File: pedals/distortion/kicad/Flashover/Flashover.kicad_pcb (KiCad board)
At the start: 2 copper layers, 84 x 84 mm, 95 parts, among them J1 Input, J2 Output, J3 9V DC, J4 SWD, J5 MIDI In, J6 MIDI Out, J7 To control board, K1 G6K-2F-Y 5VDC, K2 G6K-2F-Y 5VDC, Q1 MMBT3904, Q2 MMBT3904, SW5 Footswitch, U1 LM741, U11 H11L1, U2 TL072, U3 L7805, U4 RP2040, U5 W25Q16JVSS, U6 AP2112K-3.3, U7 MCP45HV51-104, U8 MCP45HV51-103, U9 MCP45HV51-103, Y1 12MHz

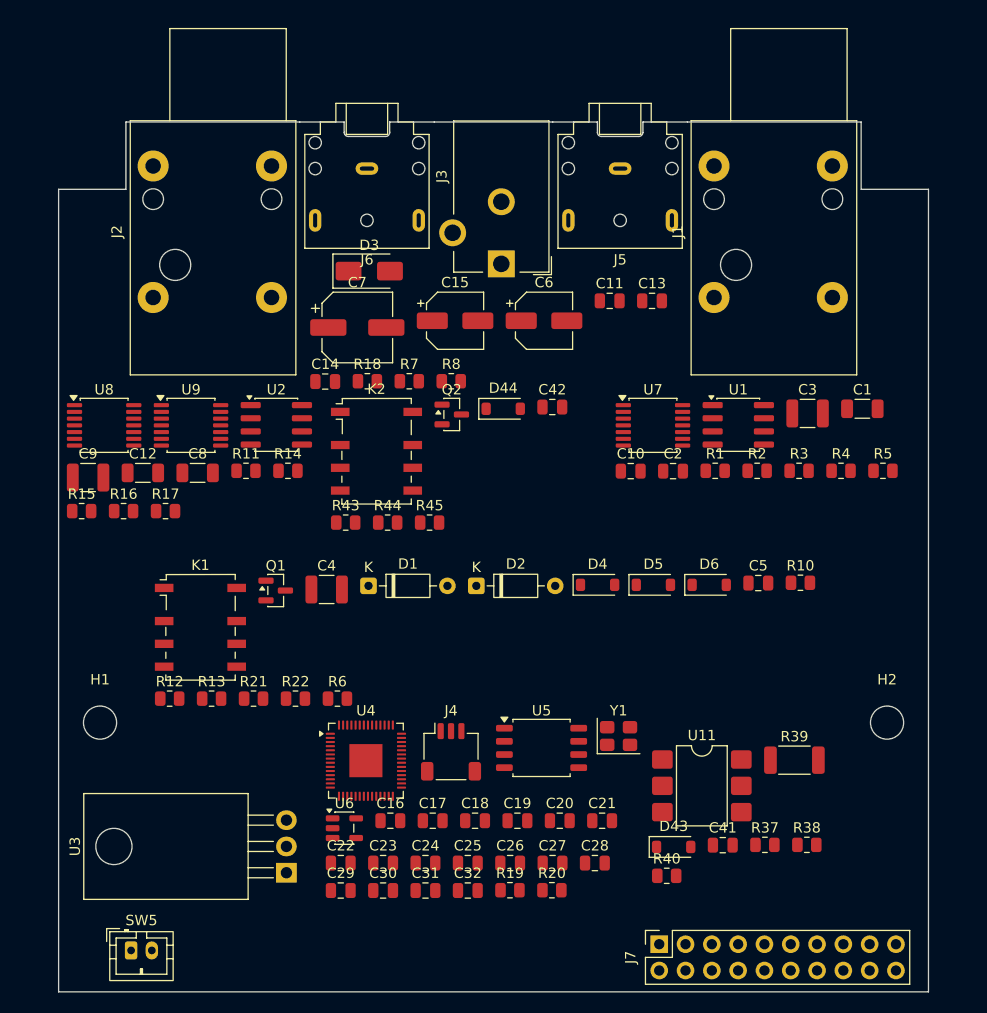
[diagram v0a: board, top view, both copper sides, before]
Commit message: Route Flashover boards (partial); add status note
Both boards now 4-layer with inner ground (and +5V) planes, JLCPCB-style
rules and net classes, ground/+5V via fan-out and autorouted signals.
Control board: 7 connections open.  Main board: 50 open; to be finished
by hand.  See pedals/distortion/kicad/FLASHOVER_STATUS.md.

Co-Authored-By: Claude Opus 5.5 <noreply@anthropic.com>
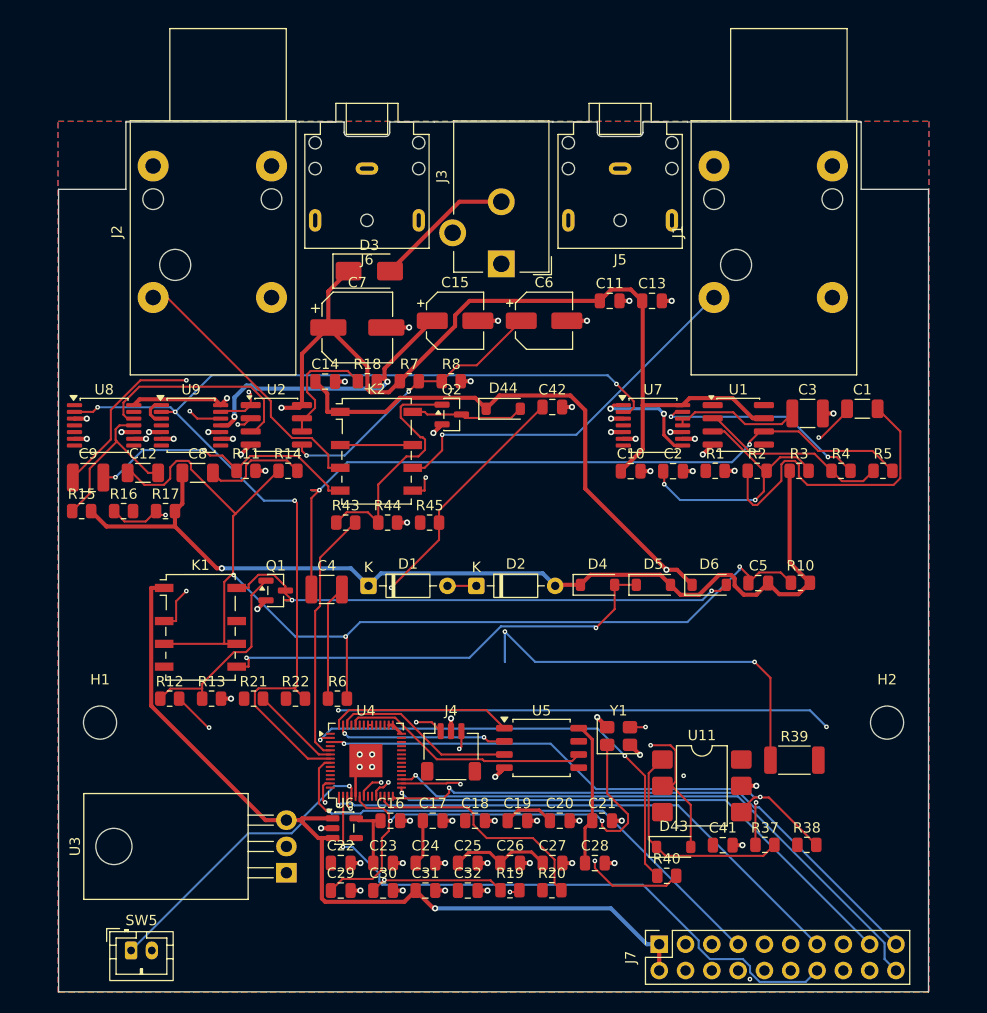
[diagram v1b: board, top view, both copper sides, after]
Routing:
- net +5V: track 0.00 -> 170.9 mm, vias 0 -> 2
- net +9V: track 0.00 -> 148.0 mm, vias 0 -> 2
- net VB: track 0.00 -> 143.7 mm, vias 0 -> 3
- net SCL: track 0.00 -> 109.5 mm, vias 0 -> 4
- net /Clipping/CLIP: track 0.00 -> 108.2 mm, vias 0 -> 3
- net Net-(J6-PadR): track 0.00 -> 90.3 mm, vias 0 -> 2
- net Net-(J6-PadT): track 0.00 -> 83.2 mm, vias 0 -> 1
- net LEVEL_SW: track 0.00 -> 80.8 mm, vias 0 -> 3
- net FOOTSW: track 0.00 -> 73.3 mm, vias 0 -> 2
- net /Clipping/GAIN_OUT: track 0.00 -> 72.4 mm, vias 0 -> 2
- net Net-(D43-A): track 0.00 -> 68.2 mm, vias 0 -> 1
- net GND: track 0.00 -> 68.0 mm, vias 0 -> 60
- net Net-(J5-PadR): track 0.00 -> 64.8 mm, vias 0 -> 1
- net LEVEL_B: track 0.00 -> 57.8 mm, vias 0 -> 1
- net LINK_LED: track 0.00 -> 56.6 mm, vias 0 -> 1
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- added copper zone on B.Cu, net GND
- added copper zone on F.Cu, net GND
- added copper zone on In1.Cu, net GND
- added copper zone on In2.Cu, net GND
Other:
- copper layers 2 -> 4

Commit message: Fit Flashover to the 1590BB and part datasheets
- Correct PEC11R encoder footprint (legs 13.2 mm apart) in a new
  GreywireStudio footprint library; swap it onto the control board and
  bend three tracks around the wider legs
- Move MIDI jacks to the side walls, spread the top jacks out and put
  their fronts against the wall; re-autoroute the main board
- gen_pcb.py rebuilds the control board only with --controls
- Add fit check, board heights and drilling guide to the status note;
  update the product document

Co-Authored-By: Claude Opus 5.5 <noreply@anthropic.com>
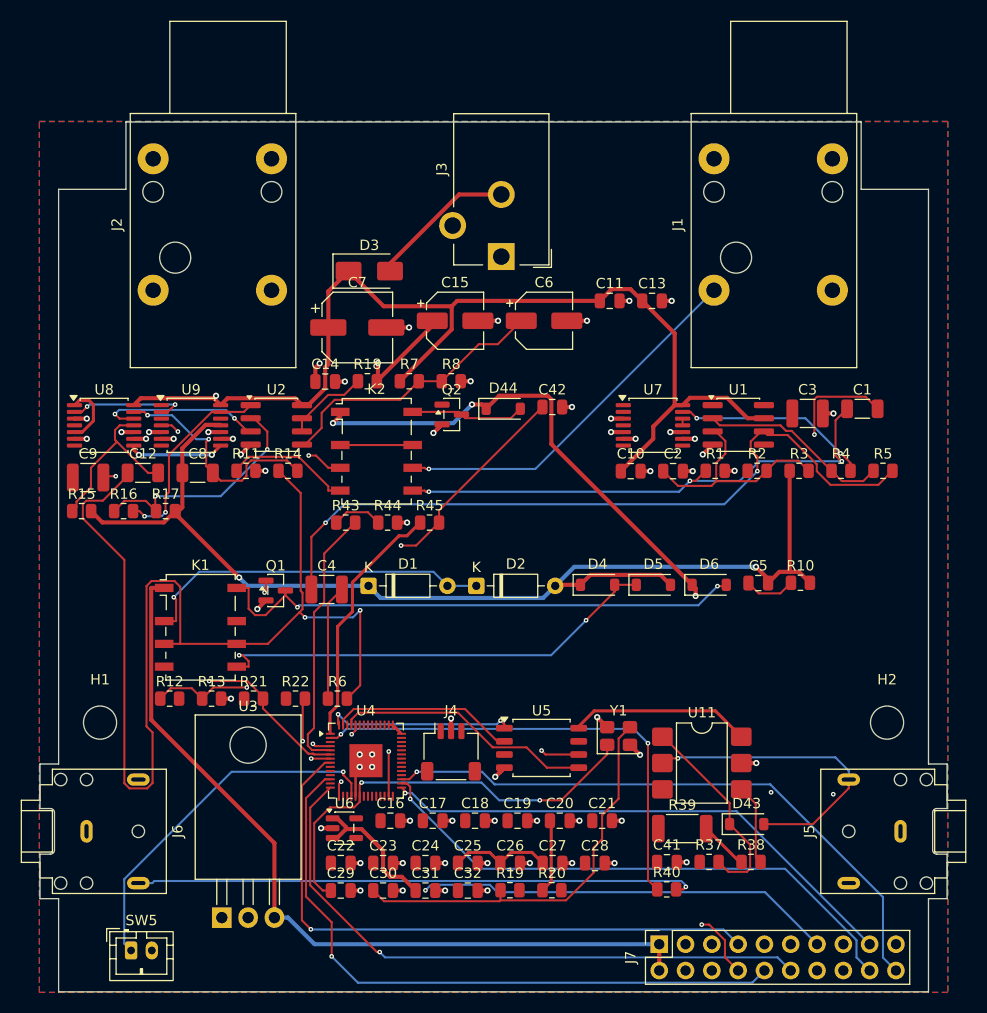
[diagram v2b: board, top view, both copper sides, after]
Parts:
- moved J5 69.5 mm to (186.3, 122.5), turned to 90 degrees
- moved J6 69.5 mm to (107.7, 122.5), turned to -90 degrees
- moved R39 12.7 mm to (165.2, 122.2)
- moved U3 7.60 mm to (120.8, 130.8), turned to 0 degrees
- moved D43 7.39 mm to (171.4, 121.8)
- moved R37 5.64 mm to (167.8, 125.5)
- moved C41 5.64 mm to (163.7, 125.5)
- moved R38 5.64 mm to (171.9, 125.5)
- moved U11 2.20 mm to (167.1, 115.9)
- moved R40 1.31 mm to (163.7, 128.1)
- moved J1 0.70 mm to (168.3, 70.2)
- moved J2 0.70 mm to (114.1, 70.2)
- moved J3 0.70 mm to (147.8, 67.0)
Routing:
- net Net-(J6-PadR): track 90.3 -> 0.00 mm, vias 2 -> 0
- net SCL: track 109.5 -> 19.7 mm
- net LEVEL_SW: track 80.8 -> 0.00 mm, vias 3 -> 0
- net Net-(J5-PadR): track 64.8 -> 0.00 mm, vias 1 -> 0
- net TONE_A: track 1.75 -> 62.7 mm
- net TONE_SW: track 0.00 -> 60.1 mm, vias 0 -> 1
- net LEVEL_B: track 57.8 -> 0.00 mm, vias 1 -> 0
- net LED_EN: track 55.6 -> 0.00 mm, vias 1 -> 0
- net LED_SCL: track 5.77 -> 54.4 mm
- net MIDI_RX: track 53.6 -> 7.78 mm, vias 2 -> 0
- net FX_IN: track 6.50 -> 50.5 mm, vias 2 -> 3
- net Net-(D43-A): track 68.2 -> 30.1 mm
- net SDA: track 8.73 -> 42.5 mm, vias 0 -> 2
- net Net-(J6-PadT): track 83.2 -> 54.4 mm
- net Net-(D1-A): track 7.25 -> 34.3 mm
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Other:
- board size 84 x 84 mm -> 87.6 x 84 mm

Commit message: Hand-route two Flashover main board connections; note progress
Connect Net-(C1-Pad2) and Net-(C3-Pad1) by hand (62 -> 60 open) and
record the next steps, including the planned route for the boxed-in
C9 connection, in FLASHOVER_STATUS.md.

Co-Authored-By: Claude Opus 5.5 <noreply@anthropic.com>
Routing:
- net Net-(C3-Pad1): track 0.65 -> 15.9 mm, vias 0 -> 2
- net Net-(C1-Pad2): track 10.1 -> 20.4 mm, vias 1 -> 2
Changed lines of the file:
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@@
+	)
+	(segment
+		(start 175.85 80.35)
+		(end 175.85 82.145)
+		(width 0.2)
+		(layer "F.Cu")
+		(net "Net-(C3-Pad1)")
+	)
+	(segment
+		(start 166.195 83.295)
+		(end 166.5 83.6)
+		(width 0.2)
+		(layer "F.Cu")
+		(net "Net-(C3-Pad1)")
+	)
+	(segment
+		(start 165.2575 83.295)
+		(end 166.195 83.295)
+		(width 0.2)
+		(layer "F.Cu")
+		(net "Net-(C3-Pad1)")
 	)
 	(segment
@@
 	)
 	(segment
+		(start 175.6 80.1)
+		(end 175.85 80.35)
+		(width 0.2)
+		(layer "F.Cu")
+		(net "Net-(C3-Pad1)")
+	)
+	(via
+		(at 175.6 80.1)
+		(size 0.45)
+		(drill 0.2)
+		(layers "F.Cu" "B.Cu")
+		(net "Net-(C3-Pad1)")
+	)
+	(via
+		(at 166.5 83.6)
+		(size 0.45)
+		(drill 0.2)
+		(layers "F.Cu" "B.Cu")
+		(net "Net-(C3-Pad1)")
+	)
+	(segment
+		(start 168.452748 80.1)
+		(end 175.6 80.1)
+		(width 0.2)
+		(layer "B.Cu")
+		(net "Net-(C3-Pad1)")
+	)
+	(segment
+		(start 166.1432 83.2432)
+		(end 166.1432 82.409548)
+		(width 0.2)
+		(layer "B.Cu")
+		(net "Net-(C3-Pad1)")
+	)
+	(segment
+		(start 166.5 83.6)
+		(end 166.1432 83.2432)
+		(width 0.2)
+		(layer "B.Cu")
+		(net "Net-(C3-Pad1)")
+	)
+	(segment
+		(start 166.1432 82.409548)
+		(end 168.452748 80.1)
+		(width 0.2)
+		(layer "B.Cu")
+		(net "Net-(C3-Pad1)")
+	)
+	(segment
 		(start 165.2575 81.995)
 		(end 166.0069 81.995)
@@
 	)
 	(segment
+		(start 171.5425 86.7425)
+		(end 170.8 86)
+		(width 0.2)
+		(layer "F.Cu")
+		(net "Net-(C1-Pad2)")
+	)
+	(segment
 		(start 178.2323 80.5314)
 		(end 177.9723 80.7914)
@@
 	)
 	(segment
+		(start 171.5425 87.685)
+		(end 171.5425 86.7425)
+		(width 0.2)
+		(layer "F.Cu")
+		(net "Net-(C1-Pad2)")
+	)
+	(segment
 		(start 184.09 81.695)
 		(end 182.9264 80.5314)
@@
 		(net "Net-(C1-Pad2)")
 	)
+	(via
+		(at 170.8 86)
+		(size 0.45)
+		(drill 0.2)
+		(layers "F.Cu" "B.Cu")
+		(net "Net-(C1-Pad2)")
+	)
+	(segment
+		(start 177.6006 83.8)
+		(end 177.989 84.1884)
+		(width 0.2)
+		(layer "B.Cu")
+		(net "Net-(C1-Pad2)")
+	)
+	(segment
+		(start 170.8 86)
+		(end 173 83.8)
+		(width 0.2)
+		(layer "B.Cu")
+		(net "Net-(C1-Pad2)")
+	)
+	(segment
+		(start 173 83.8)
+		(end 177.6006 83.8)
+		(width 0.2)
+		(layer "B.Cu")
+		(net "Net-(C1-Pad2)")
+	)

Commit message: Hand-route FX_OUT on the Flashover main board; note progress
Co-Authored-By: Claude Opus 5.5 <noreply@anthropic.com>
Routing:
- net FX_OUT: track 13.5 -> 25.5 mm, vias 1 -> 2
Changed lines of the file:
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@@
+	)
+	(segment
+		(start 121.335 87.6)
+		(end 122.0975 87.6)
+		(width 0.2)
+		(layer "F.Cu")
+		(net "FX_OUT")
 	)
 	(segment
 		(start 123.3557 86.333)
 		(end 122.1825 87.5062)
+		(width 0.2)
+		(layer "F.Cu")
+		(net "FX_OUT")
+	)
+	(segment
+		(start 122.0975 87.6)
+		(end 122.1825 87.685)
 		(width 0.2)
 		(layer "F.Cu")
@@
 		(net "FX_OUT")
 	)
+	(via
+		(at 121.335 87.6)
+		(size 0.45)
+		(drill 0.2)
+		(layers "F.Cu" "B.Cu")
+		(net "FX_OUT")
+	)
+	(segment
+		(start 110.5178 88.2092)
+		(end 111.127 87.6)
+		(width 0.2)
+		(layer "B.Cu")
+		(net "FX_OUT")
+	)
+	(segment
+		(start 111.127 87.6)
+		(end 121.335 87.6)
+		(width 0.2)
+		(layer "B.Cu")
+		(net "FX_OUT")
+	)

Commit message: Hand-route the boxed-in C9 connection on the Flashover main board
Co-Authored-By: Claude Opus 5.5 <noreply@anthropic.com>
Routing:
- net Net-(C9-Pad1): track 0.00 -> 19.3 mm, vias 0 -> 2
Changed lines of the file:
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@@
+	)
+	(segment
+		(start 106.37 88.335)
+		(end 106.37 86.43)
+		(width 0.2)
+		(layer "F.Cu")
+		(net "Net-(C9-Pad1)")
+	)
+	(segment
+		(start 120.622299 82.670201)
+		(end 120.6475 82.645)
+		(width 0.2)
+		(layer "F.Cu")
+		(net "Net-(C9-Pad1)")
+	)
+	(segment
+		(start 106.37 86.43)
+		(end 106.4 86.4)
+		(width 0.2)
+		(layer "F.Cu")
+		(net "Net-(C9-Pad1)")
+	)
+	(segment
+		(start 119.794351 82.670201)
+		(end 120.622299 82.670201)
+		(width 0.2)
+		(layer "F.Cu")
+		(net "Net-(C9-Pad1)")
+	)
+	(via
+		(at 106.4 86.4)
+		(size 0.45)
+		(drill 0.2)
+		(layers "F.Cu" "B.Cu")
+		(net "Net-(C9-Pad1)")
+	)
+	(via
+		(at 119.794351 82.670201)
+		(size 0.45)
+		(drill 0.2)
+		(layers "F.Cu" "B.Cu")
+		(net "Net-(C9-Pad1)")
+	)
+	(segment
+		(start 120.01 82.88585)
+		(end 119.794351 82.670201)
+		(width 0.2)
+		(layer "B.Cu")
+		(net "Net-(C9-Pad1)")
+	)
+	(segment
+		(start 120.01 84.787152)
+		(end 120.01 82.88585)
+		(width 0.2)
+		(layer "B.Cu")
+		(net "Net-(C9-Pad1)")
+	)
+	(segment
+		(start 107.655 85.145)
+		(end 119.652152 85.145)
+		(width 0.2)
+		(layer "B.Cu")
+		(net "Net-(C9-Pad1)")
+	)
+	(segment
+		(start 106.4 86.4)
+		(end 107.655 85.145)
+		(width 0.2)
+		(layer "B.Cu")
+		(net "Net-(C9-Pad1)")
+	)
+	(segment
+		(start 119.652152 85.145)
+		(end 120.01 84.787152)
+		(width 0.2)
+		(layer "B.Cu")
+		(net "Net-(C9-Pad1)")
 	)
 	(segment

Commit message: Hand-route CLIP on the Flashover main board; audio path done
Co-Authored-By: Claude Opus 5.5 <noreply@anthropic.com>
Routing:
- net /Clipping/CLIP: track 115.4 -> 155.2 mm
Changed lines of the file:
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@@
+	)
+	(segment
+		(start 134.1221 101.151)
+		(end 135.5637 102.5926)
+		(width 0.2)
+		(layer "F.Cu")
+		(net "/Clipping/CLIP")
 	)
 	(segment
@@
 		(width 0.2)
 		(layer "F.Cu")
+		(net "/Clipping/CLIP")
+	)
+	(segment
+		(start 135.5637 102.5926)
+		(end 167.5474 102.5926)
+		(width 0.2)
+		(layer "F.Cu")
+		(net "/Clipping/CLIP")
+	)
+	(segment
+		(start 167.5474 102.5926)
+		(end 171.615 98.525)
+		(width 0.2)
+		(layer "F.Cu")

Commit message: Route +1V1/+3V3 around U4's top pins; logic power uses 0.2 mm tracks
The 0.3 mm logic-power width and 0.6 mm vias can't escape the RP2040's
0.4 mm-pitch pins, so the class now uses the signal sizes.

Co-Authored-By: Claude Opus 5.5 <noreply@anthropic.com>
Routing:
- net /Controller/+1V1: track 9.89 -> 22.7 mm, vias 0 -> 2
- net +3V3: track 70.8 -> 74.4 mm
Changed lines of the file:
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@@
 	)
 	(setup
+		(stackup
+			(layer "F.SilkS"
+				(type "Top Silk Screen")
+			)
+			(layer "F.Paste"
+				(type "Top Solder Paste")
+			)
+			(layer "F.Mask"
+				(type "Top Solder Mask")
+				(thickness 0.01)
+			)
+			(layer "F.Cu"
+				(type "copper")
+				(thickness 0.035)
+			)
+			(layer "dielectric 1"
+				(type "core")
+				(thickness 0.48)
+				(material "FR4")
+				(epsilon_r 4.5)
+				(loss_tangent 0.02)
+			)
+			(layer "In1.Cu"
+				(type "copper")
+				(thickness 0.035)
+			)
+			(layer "dielectric 2"
+				(type "prepreg")
+				(thickness 0.48)
+				(material "FR4")
+				(epsilon_r 4.5)
+				(loss_tangent 0.02)
+			)
+			(layer "In2.Cu"
+				(type "copper")
+				(thickness 0.035)
+			)
+			(layer "dielectric 3"
+				(type "core")
+				(thickness 0.48)
+				(material "FR4")
+				(epsilon_r 4.5)
+				(loss_tangent 0.02)
+			)
+			(layer "B.Cu"
+				(type "copper")
+				(thickness 0.035)
+			)
+			(layer "B.Mask"
+				(type "Bottom Solder Mask")
+				(thickness 0.01)
+			)
+			(layer "B.Paste"
+				(type "Bottom Solder Paste")
+			)
+			(layer "B.SilkS"
+				(type "Bottom Silk Screen")
+			)
+			(copper_finish "None")
+			(dielectric_constraints no)
+		)
 		(pad_to_mask_clearance 0)
 		(allow_soldermask_bridges_in_footprints no)
@@
 		(capping no)
 		(filling no)
+		(zone_defaults)
 		(pcbplotparams
 			(layerselection 0x00000000_00000000_55555555_5755f5ff)
@@
 	)
 	(segment
+		(start 137.1 112.85)
+		(end 137.1 112.2375)
+		(width 0.3)
+		(layer "F.Cu")
+		(net "+3V3")
+	)
+	(segment
 		(start 155.2225 112.3673)
 		(end 156.7233 110.8665)
@@
 	)
 	(segment
+		(start 134.875 112.2375)
+		(end 135.275 112.2375)
+		(width 0.3)
+		(layer "F.Cu")
+		(net "+3V3")
+	)
+	(segment
 		(start 155.2225 112.54)
 		(end 155.2225 112.3673)
@@
 	(segment
 		(start 136.875 112.2375)
-		(end 137.275 112.2375)
+		(end 137.1 112.2375)
 		(width 0.2002)
 		(layer "F.Cu")
@@
 	)
 	(segment
+		(start 135.275 112.77136)
+		(end 135.47864 112.975)
+		(width 0.3)
+		(layer "F.Cu")
+		(net "+3V3")
+	)
+	(segment
 		(start 133.3765 101.2801)
 		(end 133.3765 98.4521)
@@
 	)
 	(segment
+		(start 135.275 112.2375)
+		(end 135.275 112.77136)
+		(width 0.3)
+		(layer "F.Cu")
+		(net "+3V3")
+	)
+	(segment
 		(start 137.275 112.2375)
 		(end 137.9856 112.9481)
@@
 	)
 	(segment
+		(start 136.975 112.975)
+		(end 137.1 112.85)
+		(width 0.3)
+		(layer "F.Cu")
+		(net "+3V3")
+	)
+	(segment
 		(start 131.2375 112.9703)
 		(end 131.2375 113.075)
@@
 	)
 	(segment
+		(start 137.1 112.2375)
+		(end 137.275 112.2375)
+		(width 0.2002)
+		(layer "F.Cu")
+		(net "+3V3")
+	)
+	(segment
 		(start 131.9401 110.3471)
 		(end 131.9401 102.7165)
@@
 	)
 	(segment
+		(start 135.47864 112.975)
+		(end 136.975 112.975)
+		(width 0.3)
+		(layer "F.Cu")
+		(net "+3V3")
+	)
+	(segment
 		(start 131.2153 112.9481)
 		(end 131.2375 112.9703)
@@
 	)
 	(segment
+		(start 136.475 112.2375)
+		(end 136.475 111.525)
+		(width 0.3)
+		(layer "F.Cu")
+		(net "/Controller/+1V1")
+	)
+	(segment
+		(start 135.3 118.4)
+		(end 135.3 119.0875)
+		(width 0.2)
+		(layer "F.Cu")
+		(net "/Controller/+1V1")
+	)
+	(segment
+		(start 134.5 111.67864)
+		(end 134.475 111.70364)
+		(width 0.3)
+		(layer "F.Cu")
+		(net "/Controller/+1V1")
+	)
+	(segment
 		(start 148.6867 124.5333)
 		(end 147.655 125.565)
@@
 	)
 	(segment
+		(start 135.374998 113.699998)
+		(end 135.5 113.699998)
+		(width 0.2)
+		(layer "F.Cu")
+		(net "/Controller/+1V1")
+	)
+	(segment
+		(start 134.475 112.8)
+		(end 135.374998 113.699998)
+		(width 0.2)
+		(layer "F.Cu")
+		(net "/Controller/+1V1")
+	)
+	(segment
+		(start 136.475 111.525)
+		(end 136.5 111.5)
+		(width 0.3)
+		(layer "F.Cu")
+		(net "/Controller/+1V1")
+	)
+	(segment
 		(start 144.5927 124.5373)
 		(end 143.565 125.565)
@@
 	)
 	(segment
+		(start 134.5 111.5)
+		(end 134.5 111.67864)
+		(width 0.3)
+		(layer "F.Cu")
+		(net "/Controller/+1V1")
+	)
+	(segment
 		(start 146.6273 124.5373)
 		(end 144.5927 124.5373)
@@
 		(net "/Controller/+1V1")
 	)
+	(segment
+		(start 136.5 111.5)
+		(end 134.5 111.5)
+		(width 0.3)
+		(layer "F.Cu")
+		(net "/Controller/+1V1")
+	)
+	(segment
+		(start 134.475 112.2375)
+		(end 134.475 112.8)
+		(width 0.2)
+		(layer "F.Cu")
+		(net "/Controller/+1V1")
+	)
+	(segment
+		(start 135.3 119.0875)
+		(end 135.275 119.1125)
+		(width 0.2)
+		(layer "F.Cu")
+		(net "/Controller/+1V1")
+	)
+	(via
+		(at 135.5 113.699998)
+		(size 0.45)
+		(drill 0.2)
+		(layers "F.Cu" "B.Cu")
+		(net "/Controller/+1V1")
+	)
+	(via
+		(at 135.3 118.4)
+		(size 0.45)
+		(drill 0.2)
+		(layers "F.Cu" "B.Cu")
+		(net "/Controller/+1V1")
+	)
+	(segment
+		(start 135.5 113.699998)
+		(end 134.7 114.499998)
+		(width 0.2)
+		(layer "B.Cu")
+		(net "/Controller/+1V1")
+	)
+	(segment
+		(start 134.7 114.499998)
+		(end 134.7 116.675448)
+		(width 0.2)
+		(layer "B.Cu")
+		(net "/Controller/+1V1")
+	)
+	(segment
+		(start 134.7 116.675448)
+		(end 133.6 117.775448)
+		(width 0.2)
+		(layer "B.Cu")
+		(net "/Controller/+1V1")
+	)
+	(segment
+		(start 133.6 118.3)
+		(end 133.7 118.4)
+		(width 0.2)
+		(layer "B.Cu")
+		(net "/Controller/+1V1")
+	)
+	(segment
+		(start 133.6 117.775448)
+		(end 133.6 118.3)
+		(width 0.2)
+		(layer "B.Cu")
+		(net "/Controller/+1V1")
+	)
+	(segment
+		(start 133.7 118.4)
+		(end 135.3 118.4)
+		(width 0.2)
+		(layer "B.Cu")
+		(net "/Controller/+1V1")
+	)
